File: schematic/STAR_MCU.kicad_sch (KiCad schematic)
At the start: 153 parts, among them J1 EMU CFG, J10 Conn_01x04, J11 6120XX21621_61200621621, J12 Conn_01x04, J13 6120XX21621_61200821621, J14 6120XX21621_61200821621, J15 6120XX21621_61200821621, J16 6120XX21621_61200821621, J18 6120XX21621_61200621621, J19 6120XX21621_61200821621, J2 USB4216-03-A, J20 S5B-XH-A, J21 6120XX21621_61200621621, J3 UPSEL_CFG, J4 E1E2-Emulator-Interface, J7 USB4216-03-A, J8 Conn_02x20_Odd_Even, J9 Conn_01x09, SW1 OP_CFG, U1 R5F572NNHGFP-30, U2 CY7C65213A-28PVXI, U3 TVS2200DRV, U4 LDL1117S33R, U5 TPS2116DRLR, U6 TVS2200DRV, Y1 24MHz

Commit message: current status
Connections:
- net ESP_PI_SPI3_PM_CIPO is gone; now on net RPI5_RSPIA_CIPO: J8.21 (Pin_21)
- net ESP_PI_SPI3_PM_COPI is gone; now on net RPI5_RSPIA_COPI: J8.19 (Pin_19)
- net ESP_PI_SPI3_PM_CS is gone; now on net RPI5_RSPIA_CS: J8.24 (Pin_24)
- net ESP_PI_SPI3_PM_SCLK is gone; now on net RPI5_RSPIA_SCLK: J8.23 (Pin_23)
- net RSPIC_MOTOR0_nCS: now also U1.29 (P17)
- net RSPIC_MOTOR1_nCS: now also U1.25 (P23)
- net RSPIC_MOTOR2_nCS: now also U1.18 (P32)
- net RSPIC_MOTOR3_nCS: now also U1.70 (PA0)
- net ESP_PI_SPI3_PM_DRDY1: no longer names the net of J8.38 (Pin_38)
- net ESP_PI_SPI3_PM_DRDY2: no longer names the net of J8.40 (Pin_40)
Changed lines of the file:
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@@
 	(wire
 		(pts
-			(xy 139.7 88.9) (xy 91.44 88.9)
-		)
-		(stroke
-			(width 0)
-			(type default)
-		)
-	)
-	(wire
-		(pts
 			(xy 427.99 190.5) (xy 443.23 190.5)
 		)
@@
 	(wire
 		(pts
-			(xy 91.44 91.44) (xy 139.7 91.44)
-		)
-		(stroke
-			(width 0)
-			(type default)
-		)
-	)
-	(wire
-		(pts
 			(xy 401.32 204.47) (xy 401.32 210.82)
 		)
@@
 		)
 	)
-	(label "ESP_PI_SPI3_PM_SCLK"
-		(at 29.21 71.12 0)
-		(effects
-			(font
-				(size 1.27 1.27)
-			)
-			(justify left bottom)
-		)
-	)
 	(label "SCI9_TXD9"
 		(at 354.33 226.06 0)
@@
 		)
 	)
+	(label "RSPIC_MOTOR0_nCS"
+		(at 593.09 342.9 0)
+		(effects
+			(font
+				(size 1.27 1.27)
+			)
+			(justify left bottom)
+		)
+	)
 	(label "EMU_TMS"
 		(at 593.09 314.96 0)
@@
 		)
 	)
+	(label "RSPIC_MOTOR1_nCS"
+		(at 593.09 331.47 0)
+		(effects
+			(font
+				(size 1.27 1.27)
+			)
+			(justify left bottom)
+		)
+	)
 	(label "EMU_TDI_RXD"
 		(at 351.79 336.55 0)
@@
 		)
 	)
+	(label "RSPIC_MOTOR3_nCS"
+		(at 722.63 288.29 180)
+		(effects
+			(font
+				(size 1.27 1.27)
+			)
+			(justify right bottom)
+		)
+	)
 	(label "PMOD_JB_INT1"
 		(at 722.63 341.63 180)
@@
 		)
 	)
-	(label "ESP_PI_SPI3_PM_CIPO"
-		(at 29.21 68.58 0)
-		(effects
-			(font
-				(size 1.27 1.27)
-			)
-			(justify left bottom)
-		)
-	)
 	(label "USB0_USBC_VBUS"
 		(at 266.7 165.1 180)
@@
 		)
 	)
-	(label "MOTOR1_EN"
-		(at 722.63 266.7 180)
+	(label "RPI5_RSPIA_COPI"
+		(at 29.21 66.04 0)
 		(effects
 			(font
 				(size 1.27 1.27)
 			)
-			(justify right bottom)
+			(justify left bottom)
 		)
 	)
-	(label "ENCODER1_PHASE_A"
-		(at 722.63 334.01 180)
+	(label "MOTOR1_EN"
+		(at 722.63 266.7 180)
 		(effects
 			(font
@@
 		)
 	)
-	(label "ESP_PI_SPI3_PM_DRDY2"
-		(at 139.7 91.44 180)
+	(label "ENCODER1_PHASE_A"
+		(at 722.63 334.01 180)
 		(effects
 			(font
@@
 		)
 	)
+	(label "RPI5_RSPIA_SCLK"
+		(at 29.21 71.12 0)
+		(effects
+			(font
+				(size 1.27 1.27)
+			)
+			(justify left bottom)
+		)
+	)
 	(label "RSPIC_COPI"
 		(at 722.63 247.65 180)
@@
 		)
 	)
+	(label "RPI5_RSPIA_CS"
+		(at 139.7 71.12 180)
+		(effects
+			(font
+				(size 1.27 1.27)
+			)
+			(justify right bottom)
+		)
+	)
 	(label "P3V3_MOTOR_DRIVER"
 		(at 676.91 443.23 0)
@@
 		)
 	)
-	(label "ESP_PI_SPI3_PM_DRDY1"
-		(at 139.7 88.9 180)
-		(effects
-			(font
-				(size 1.27 1.27)
-			)
-			(justify right bottom)
-		)
-	)
 	(label "MOTOR0_nFAULT"
 		(at 722.63 233.68 180)
@@
 		)
 	)
+	(label "RPI5_RSPIA_CIPO"
+		(at 29.21 68.58 0)
+		(effects
+			(font
+				(size 1.27 1.27)
+			)
+			(justify left bottom)
+		)
+	)
 	(label "ENCODER0_PHASE_A"
 		(at 593.09 328.93 0)
@@
 		)
 	)
-	(label "ESP_PI_SPI3_PM_CS"
-		(at 139.7 71.12 180)
+	(label "RSPIC_SCLK"
+		(at 722.63 252.73 180)
 		(effects
 			(font
@@
 		)
 	)
-	(label "RSPIC_SCLK"
-		(at 722.63 252.73 180)
+	(label "RSPIC_MOTOR2_nCS"
+		(at 593.09 312.42 0)
 		(effects
 			(font
 				(size 1.27 1.27)
 			)
-			(justify right bottom)
+			(justify left bottom)
 		)
 	)
@@
 		)
 	)
-	(label "ESP_PI_SPI3_PM_COPI"
-		(at 29.21 66.04 0)
-		(effects
-			(font
-				(size 1.27 1.27)
-			)
-			(justify left bottom)
-		)
-	)

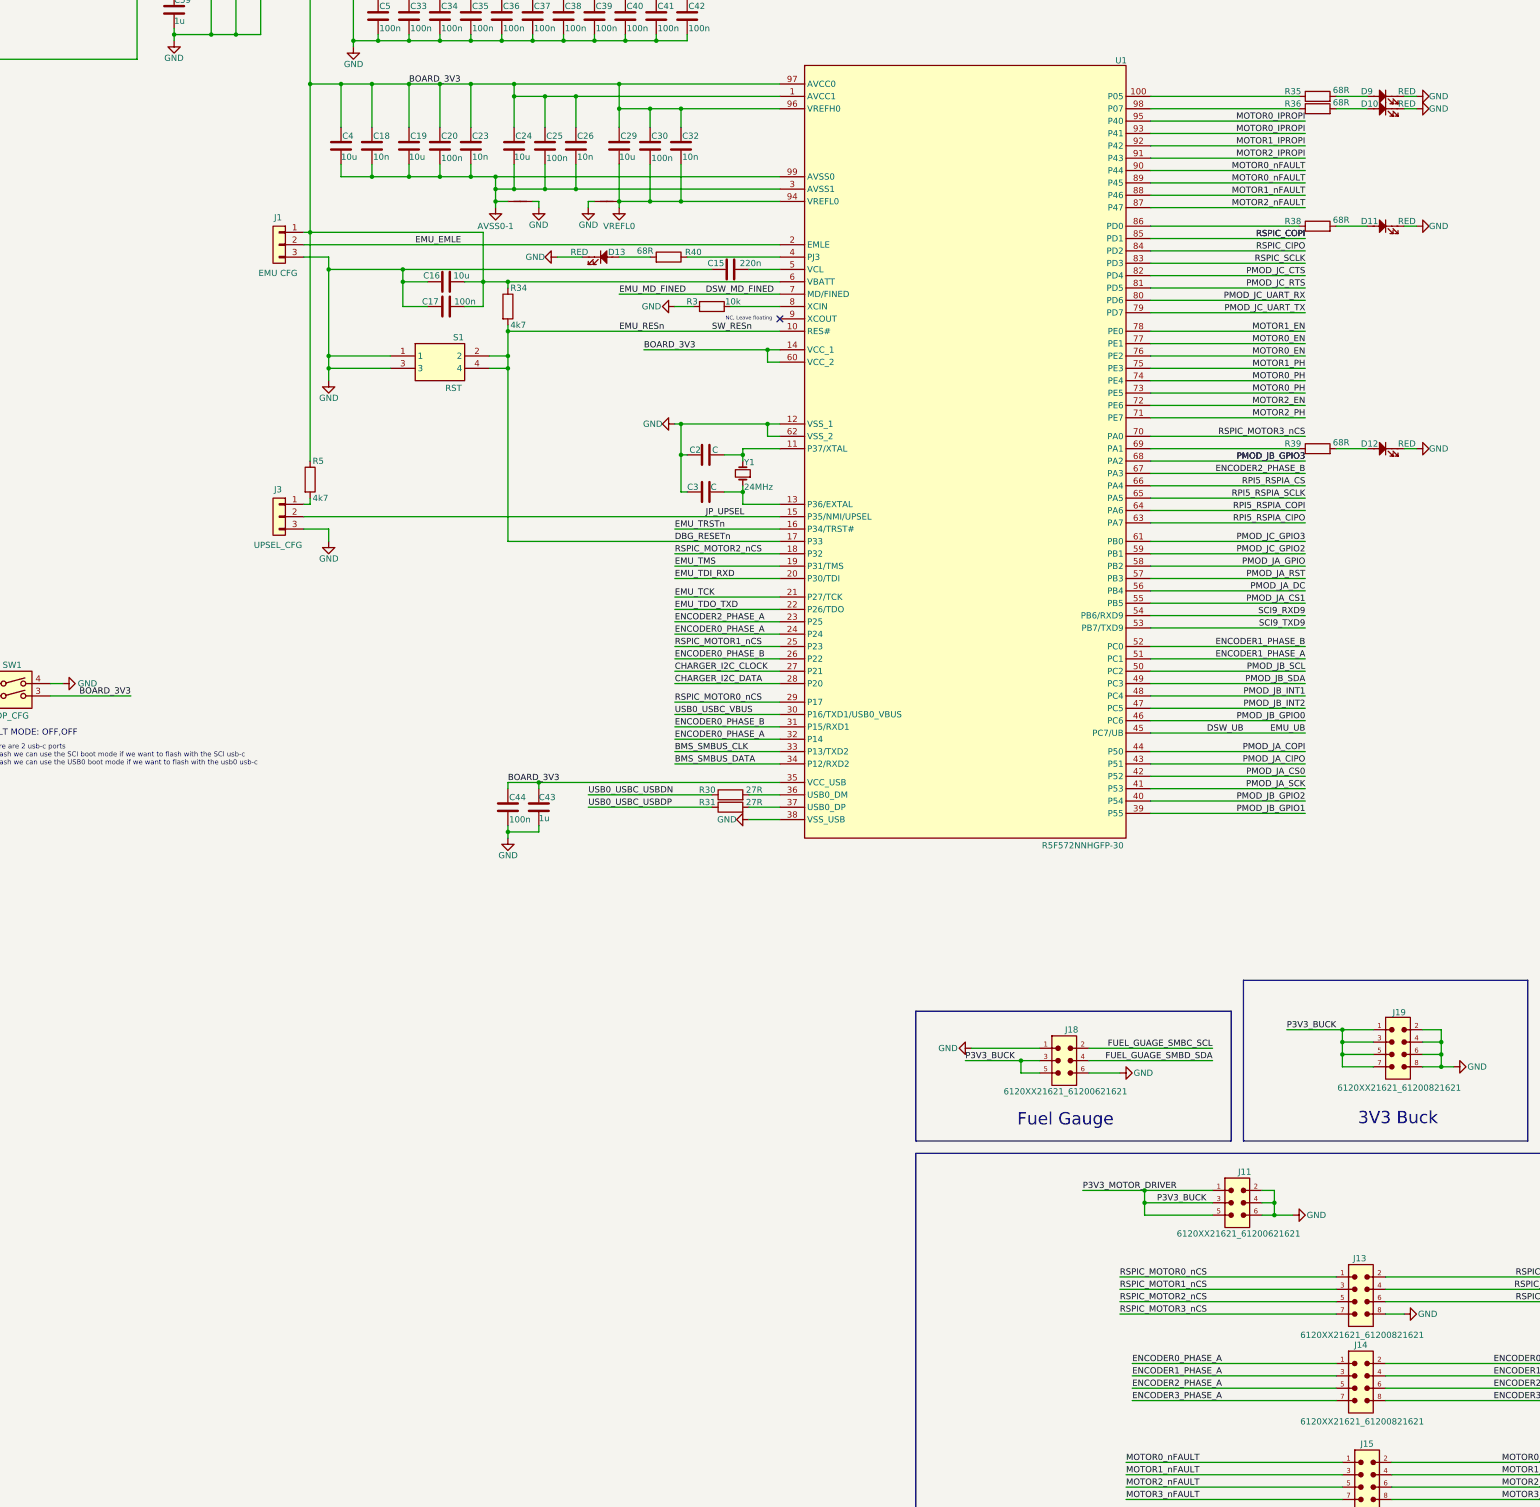
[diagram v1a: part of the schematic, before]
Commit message: reorganize PMOD connectors and add status LEDs
- PMOD JA: reorder pins 7-10 (DC, RST, GPIO, CS1) for standard display compatibility
- PMOD JB: change from I2C to 6-pin GPIO (PC6, P55, P54, PA2)
- PMOD JC: change from UART to 6-pin I2C with interrupts (PC4, PC5, PC2, PC3)
- PMOD JD: add new 6-pin GPIO expansion (PD7, PD6, PD5, PD4)
- Add ERROR_STATUS_LED (PB1) and SYSTEM_HEARTBEAT_LED (PB0)
- Add SAMTEC SSW-106-02-G-D-RA and SSW-106-02-G-S-RA connector libraries
- Update schematic labels, documentation tables, and netclass colors
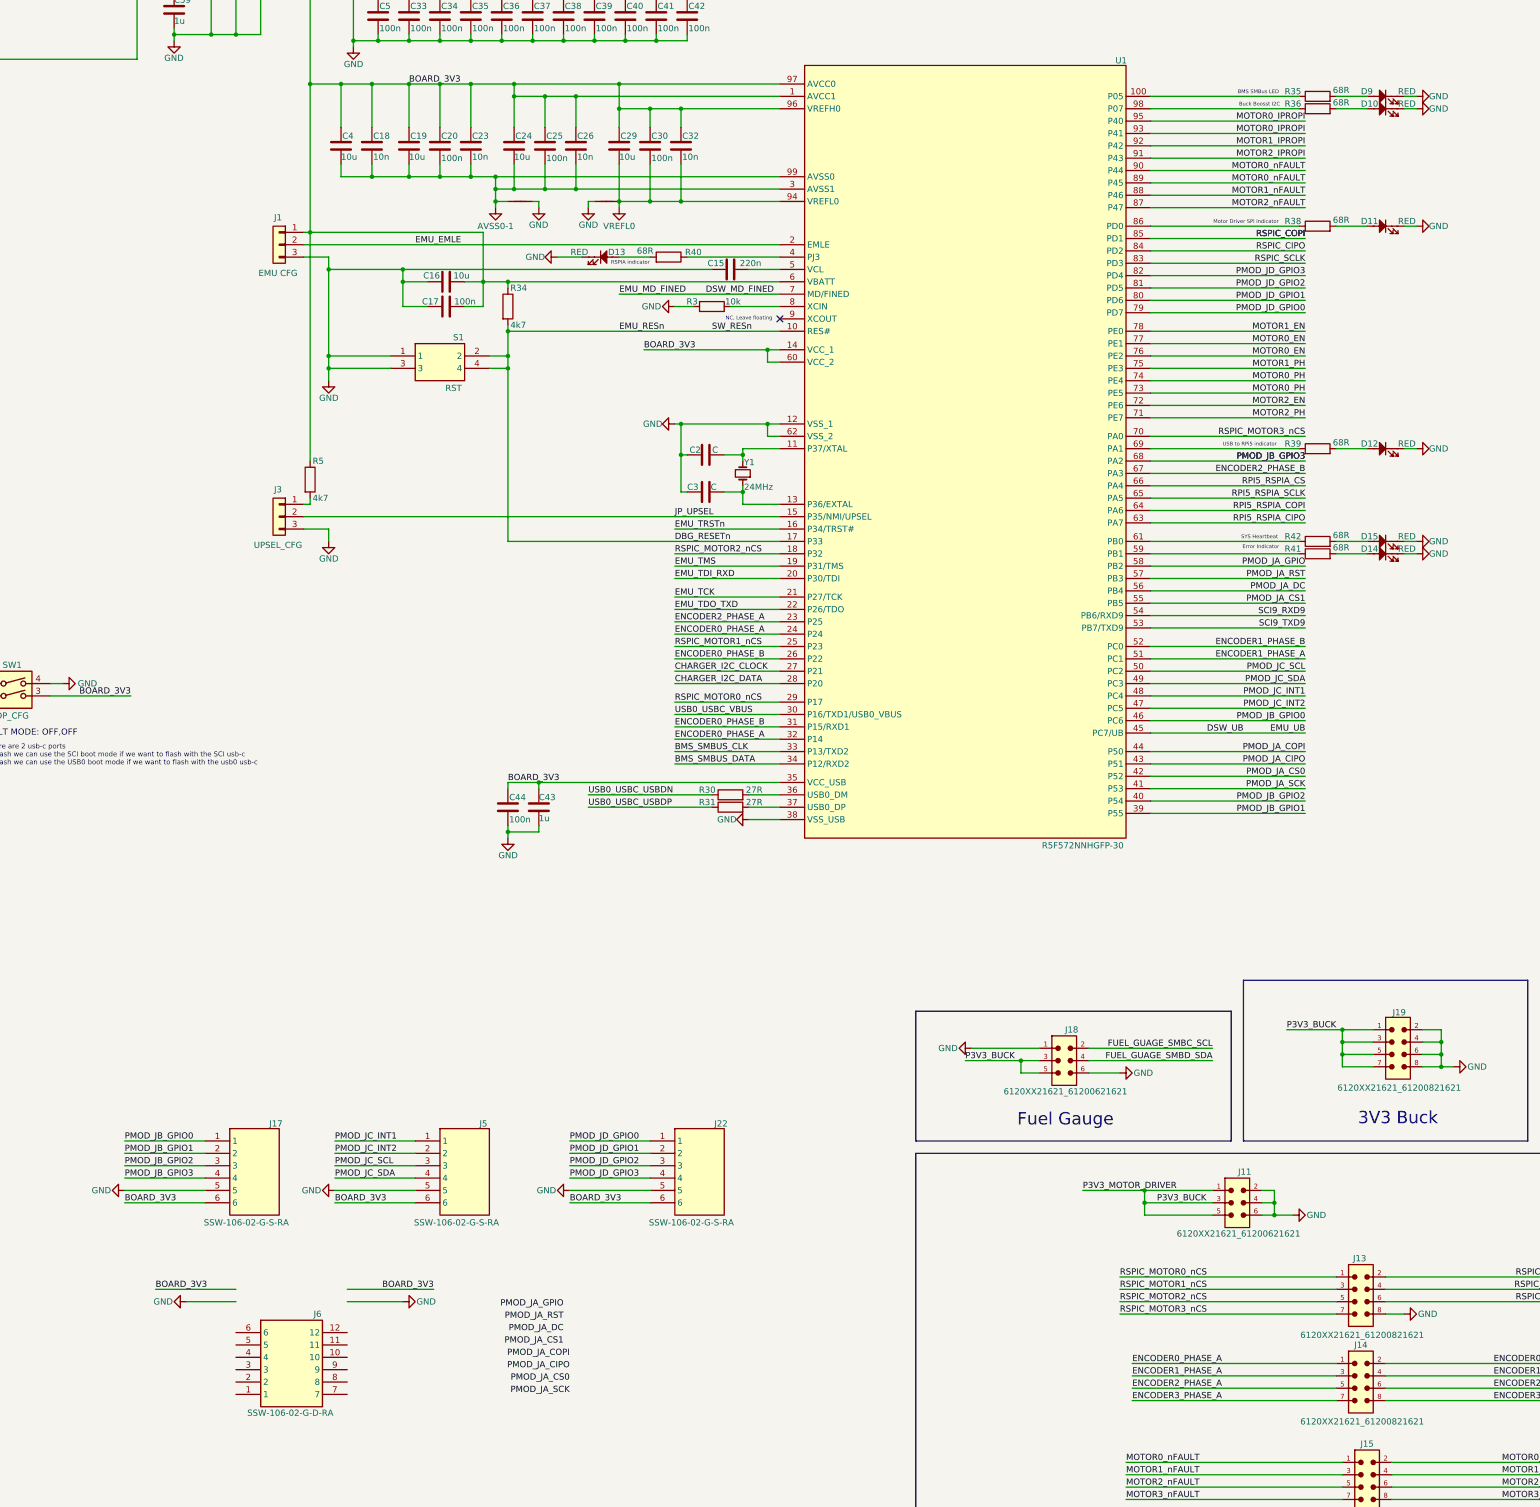
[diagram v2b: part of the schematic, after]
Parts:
- added D14, D15: RED, SML-D12Y1WT86:LEDC1608X55N, symbol PCM_SL_Devices:LED
- added J17, J22, J5: SSW-106-02-G-S-RA, SSW-106-XX-YYY-S-RA, symbol SSW-106-02-G-S-RA:SSW-106-02-G-S-RA
- added J6: SSW-106-02-G-D-RA, SSW10602GDRA, symbol SSW-106-02-G-D-RA:SSW-106-02-G-D-RA
- added R41, R42: 68R, Resistor_SMD:R_0603_1608Metric_Pad0.98x0.95mm_HandSolder, symbol Device:R
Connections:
- net BOARD_3V3: now also J17.6, J22.6, J5.6
- net GND: now also D14.1, D15.1, J17.5, J22.5, J5.5
- net PMOD_JB_GPIO0: now also J17.1
- net PMOD_JB_GPIO1: now also J17.2
- net PMOD_JB_GPIO2: now also J17.3
- net PMOD_JB_GPIO3: now also J17.4
- net PMOD_JB_INT1 renamed PMOD_JC_INT1
- net PMOD_JC_INT1: now also J5.1
- net PMOD_JB_INT2 renamed PMOD_JC_INT2
- net PMOD_JC_INT2: now also J5.2
- net PMOD_JB_SCL renamed PMOD_JC_SCL
- net PMOD_JC_SCL: now also J5.3
- net PMOD_JB_SDA renamed PMOD_JC_SDA
- net PMOD_JC_SDA: now also J5.4
- net PMOD_JC_CTS renamed PMOD_JD_GPIO3
- net PMOD_JD_GPIO3: now also J22.4
- net PMOD_JC_GPIO2: no longer names the net of U1.59 (PB1)
- net PMOD_JC_GPIO2: now also R41.1
- net PMOD_JC_GPIO3: no longer names the net of U1.61 (PB0)
- net PMOD_JC_GPIO3: now also R42.1
- net PMOD_JC_RTS renamed PMOD_JD_GPIO2
- net PMOD_JD_GPIO2: now also J22.3
- net PMOD_JC_UART_RX renamed PMOD_JD_GPIO1
- net PMOD_JD_GPIO1: now also J22.2
- net PMOD_JC_UART_TX renamed PMOD_JD_GPIO0
- net PMOD_JD_GPIO0: now also J22.1
- new net: D15.2, R42.2
- new net: D14.2, R41.2
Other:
- note added: "BMS SMBus LED"
- note added: "Buck Boosst I2C"
- note added: "Error Indicator"
- note added: "Motor Driver SPI indicator"
- note added: "RSPIA indicator"
- note added: "SYS Heartbeat"
- note added: "USB to RPi5 indicator"

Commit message: MCU
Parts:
- added J23: Conn_02x20_Odd_Even, Connector_PinHeader_2.54mm:PinHeader_2x20_P2.54mm_Vertical, symbol Connector_Generic:Conn_02x20_Odd_Even
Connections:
- net BOARD_3V3: now also J6.12, J6.6
- net GND: now also J6.11, J6.5, J23.14 (Pin_14), J23.20 (Pin_20), J23.25 (Pin_25), J23.30 (Pin_30), J23.34 (Pin_34), J23.39 (Pin_39), J23.6 (Pin_6), J23.9 (Pin_9)
- net PMOD_JA_CIPO: now also J6.3
- net PMOD_JA_COPI: now also J6.2
- net PMOD_JA_CS0: now also J6.1
- net PMOD_JA_CS1: now also J6.10
- net PMOD_JA_DC: now also J6.7
- net PMOD_JA_GPIO: now also J6.9
- net PMOD_JA_RST: now also J6.8
- net PMOD_JA_SCK: now also J6.4
- net PI_INTERNAL_3V3: now reaches J8.1 (Pin_1)
- net PI_INTERNAL_3V3: now also J8.17 (Pin_17), J23.1 (Pin_1), J23.17 (Pin_17)
- net PI_INTERNAL_5V0: now reaches J8.2 (Pin_2)
- net PI_INTERNAL_5V0: now also J8.4 (Pin_4), J23.2 (Pin_2), J23.4 (Pin_4)
- no-connect marks 24 -> 66
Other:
- note added: "MCU"
- note added: "PMOD"
- note removed: "*** TODO: This wont work with a hat ***"
- note removed: "MALE"
- moved on the sheet: C1, C10, C11, C12, C13, C14, C15, C16, C17, C18, C19, C2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

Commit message: Replace LED pins and charger I2C with PMODs and DS18B20+ sensor
Hardware Changes:
- Remove all 7 LED pin assignments (activity indicators)
- Remove battery charger I2C lines (P20/P21 SCL1/SDA1)
- Add DS18B20+ 1-Wire temperature sensor on P05 (pin 100)
- Create PMOD JE (6-pin GPIO) using PJ3, PB1, PB0, PA1
- Create PMOD JF (6-pin GPIO/I2C) using PD0, P07, P21, P20

Documentation Updates:
- Update color legend: remove LED/charger, add PMOD JE/JF/temp sensor
- Update all 9 pin table entries with new functions
- Add PMOD JE table (4x IRQ-capable GPIO pins)
- Add PMOD JF table (4x GPIO with optional RIIC1 I2C)
- Add DS18B20+ temperature sensor section with specs and wiring
- Update PCB layout recommendations for new PMODs

Schematic Updates:
- Change CHARGER_I2C_DATA → PMOD_JF_GPIO3
- Change CHARGER_I2C_CLOCK → PMOD_JF_GPIO2

Netclass Configuration:
- Add PMOD JE netclass (orange: rgb(255, 165, 0))
- Add PMOD JF netclass (teal: rgb(0, 128, 128))
- Add Temperature Sensor netclass (light green: rgb(144, 238, 144))
- Remove Status LEDs netclass patterns
- Add /PMOD_JE_*, /PMOD_JF_*, /DS18B20_DQ patterns

Pin Allocations:
  PMOD JE (GPIO): PJ3, PB1, PB0, PA1 (pins 4, 59, 61, 69)
  PMOD JF (GPIO/I2C): PD0, P07, P21, P20 (pins 86, 98, 27, 28)
  DS18B20+ DQ: P05 (pin 100, IRQ13 capable)

Total PMODs: 6 (JA=SPI, JB=GPIO, JC=I2C, JD=GPIO, JE=GPIO, JF=GPIO/I2C)
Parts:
- added J24, J25, J26, J27, J28, J29, J30: HC-SR04, Connector_PinSocket_2.54mm:PinSocket_1x04_P2.54mm_Vertical, symbol Connector:Conn_01x04_Socket
- added R43: 10k, Resistor_SMD:R_0603_1608Metric_Pad0.98x0.95mm_HandSolder, symbol Device:R
- added U7: DS18B20+, DS18B20, symbol DS188B20+:DS18B20+
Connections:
- net GND: now also J24.4 (Pin_4), J25.4 (Pin_4), J26.4 (Pin_4), J27.4 (Pin_4), J28.4 (Pin_4), J29.4 (Pin_4), J30.4 (Pin_4), U7.1 (GND)
- net P3V3_BUCK: now also J24.1 (Pin_1), J25.1 (Pin_1), J26.1 (Pin_1), J27.1 (Pin_1), J28.1 (Pin_1), J29.1 (Pin_1), J30.1 (Pin_1), R43.2, U7.3 (VDD)
- net CHARGER_I2C_CLOCK renamed PMOD_JF_GPIO2
- net CHARGER_I2C_DATA renamed PMOD_JF_GPIO3
- new net HCSR04_ECHO1: J24.3 (Pin_3)
- new net HCSR04_ECHO2: J25.3 (Pin_3)
- new net HCSR04_ECHO3: J26.3 (Pin_3)
- new net HCSR04_ECHO4: J27.3 (Pin_3)
- new net HCSR04_ECHO5: J28.3 (Pin_3)
- new net HCSR04_ECHO6: J29.3 (Pin_3)
- new net HCSR04_ECHO7: J30.3 (Pin_3)
- new net HCSR04_TRIG1: J24.2 (Pin_2)
- new net HCSR04_TRIG2: J25.2 (Pin_2)
- new net HCSR04_TRIG3: J26.2 (Pin_2)
- new net HCSR04_TRIG4: J27.2 (Pin_2)
- new net HCSR04_TRIG5: J28.2 (Pin_2)
- new net HCSR04_TRIG6: J29.2 (Pin_2)
- new net HCSR04_TRIG7: J30.2 (Pin_2)
- new net TEMPERATURE_SENSOR: R43.1, U7.2 (DQ)
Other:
- note added: "SONAR"
- note added: "Temperature Sensor"
- note added: "VCC TRIG ECHO GND"

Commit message: Fix schematic labels: replace 'x' placeholders and normalize PMOD names
Schematic Label Updates:
- Replace 7 'x' placeholder labels with correct signal names:
  * 3x PMOD_JE_GPIO (0-3) - IRQ-capable GPIO expansion
  * 3x PMOD_JF_GPIO (0-1) - GPIO/I2C expansion
  * 1x DS18B20_DQ - 1-Wire temperature sensor

- Normalize PMOD label naming convention:
  * pmod-e-1 → PMOD_JE_GPIO0
  * pmod-e-2 → PMOD_JE_GPIO1
  * pmod-e-3 → PMOD_JE_GPIO2
  * pmod-e-4 → PMOD_JE_GPIO3
  * pmod-f-1 → PMOD_JF_GPIO0
  * pmod-f-2 → PMOD_JF_GPIO1
  * pmod-f-3 → PMOD_JF_GPIO2
  * pmod-f-4 → PMOD_JF_GPIO3

All schematic labels now match documentation and netclass patterns.
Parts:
- removed D10, D11, D12, D13, D14, D15, D9: RED, SML-D12Y1WT86:LEDC1608X55N, symbol PCM_SL_Devices:LED
- removed R35, R36, R38, R39, R40, R41, R42: 68R, Resistor_SMD:R_0603_1608Metric_Pad0.98x0.95mm_HandSolder, symbol Device:R
- added J31, J32: SSW-106-02-G-S-RA, SSW-106-XX-YYY-S-RA, symbol SSW-106-02-G-S-RA:SSW-106-02-G-S-RA
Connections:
- net BOARD_3V3: now also J31.6, J32.6
- net GND: now also J31.5, J32.5
- net PMOD_JF_GPIO2: now also J31.3
- net PMOD_JF_GPIO3: now also J31.4
- net PMOD_JE_GPIO2: now reaches U1.59 (PB1)
- net PMOD_JE_GPIO2: now also J32.3
- net PMOD_JF_GPIO0: now reaches U1.100 (P05)
- net PMOD_JF_GPIO0: now also J31.1
- net PMOD_JE_GPIO3: now reaches U1.4 (PJ3)
- net PMOD_JE_GPIO3: now also J32.4
- net DS18B20_DQ: now reaches U1.61 (PB0)
- net PMOD_JF_GPIO1: now reaches U1.69 (PA1)
- net PMOD_JF_GPIO1: now also J31.2
- net PMOD_JE_GPIO1: now reaches U1.86 (PD0)
- net PMOD_JE_GPIO1: now also J32.2
- net PMOD_JE_GPIO0: now reaches U1.98 (P07)
- net PMOD_JE_GPIO0: now also J32.1
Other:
- note removed: "BMS SMBus LED"
- note removed: "Buck Boosst I2C"
- note removed: "Error Indicator"
- note removed: "Motor Driver SPI indicator"
- note removed: "RSPIA indicator"
- note removed: "SYS Heartbeat"
- note removed: "USB to RPi5 indicator"
- moved on the sheet: J6, R43, U7

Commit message: Rename PMOD JF GPIO2/GPIO3 to SCL/SDA for I2C clarity
Changes to match PMOD JC I2C naming convention:

Schematic:
- PMOD_JF_GPIO2 → PMOD_JF_SCL (P21, RIIC1 SCL)
- PMOD_JF_GPIO3 → PMOD_JF_SDA (P20, RIIC1 SDA)
- Keep PMOD_JF_GPIO0/GPIO1 for PD0/P07 (non-I2C pins)

Documentation:
- Update pin table entries for pins 27 & 28
- Retitle PMOD JF: "I2C Expansion with GPIO" (was "GPIO with I2C Option")
- Update table caption: "I2C + 2x GPIO" (was "4x GPIO / I2C")
- Rewrite purpose: primary I2C, secondary GPIO
- Update compatible modules list for I2C sensors
- Update color legend: "PMOD JF (I2C + GPIO)"
- Emphasize I2C configuration with dual-bus support

This makes PMOD JF consistent with PMOD JC I2C naming:
- PMOD JC: PMOD_JC_SCL, PMOD_JC_SDA (RIIC2)
- PMOD JF: PMOD_JF_SCL, PMOD_JF_SDA (RIIC1)

Both I2C PMODs now use function-specific labels (SCL/SDA),
not generic GPIO labels.
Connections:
- net TEMPERATURE_SENSOR is gone; now on net DS18B20_DQ: R43.1, U7.2 (DQ)
- net PMOD_JF_GPIO2 renamed PMOD_JF_SCL
- net PMOD_JF_GPIO3 renamed PMOD_JF_SDA
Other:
- moved on the sheet: R43, U7
